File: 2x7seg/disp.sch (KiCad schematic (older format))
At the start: 11 parts, among them P1 CONN_01X08, P2 CONN_01X08, U1 TLC59282, U2 LDD-A814RI

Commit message: Adjust the pin drill size for the 7-seg display.
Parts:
- P1, P2: footprint Pin_Headers:Pin_Header_Straight_1x08 -> local:Pin_Header_1x08_edge
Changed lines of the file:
@@
 F 0 "P1" H 1200 2600 50  0000 C CNN
 F 1 "CONN_01X08" V 1300 2150 50  0000 C CNN
-F 2 "Pin_Headers:Pin_Header_Straight_1x08" H 1200 2150 60  0001 C CNN
+F 2 "local:Pin_Header_1x08_edge" H 1200 2150 60  0001 C CNN
 F 3 "" H 1200 2150 60  0000 C CNN
 	1    1200 2150
@@
 F 0 "P2" H 10500 2600 50  0000 C CNN
 F 1 "CONN_01X08" V 10600 2150 50  0000 C CNN
-F 2 "Pin_Headers:Pin_Header_Straight_1x08" H 10500 2150 60  0001 C CNN
+F 2 "local:Pin_Header_1x08_edge" H 10500 2150 60  0001 C CNN
 F 3 "" H 10500 2150 60  0000 C CNN
 	1    10500 2150

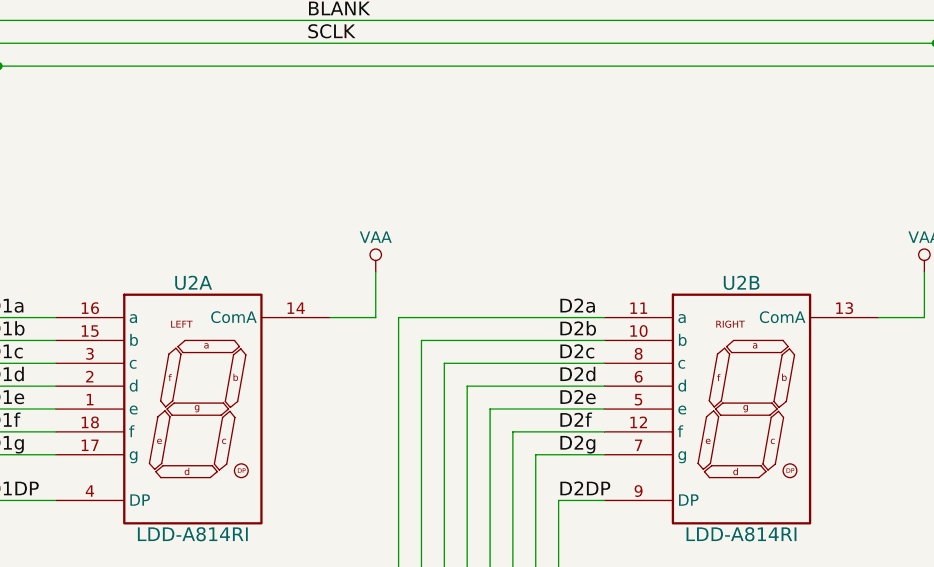
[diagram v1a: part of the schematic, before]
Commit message: Adjust the silk screen a little. Move some vias out of back silkscreen. Stitch in some more ground fill. Upload to OSHPark.
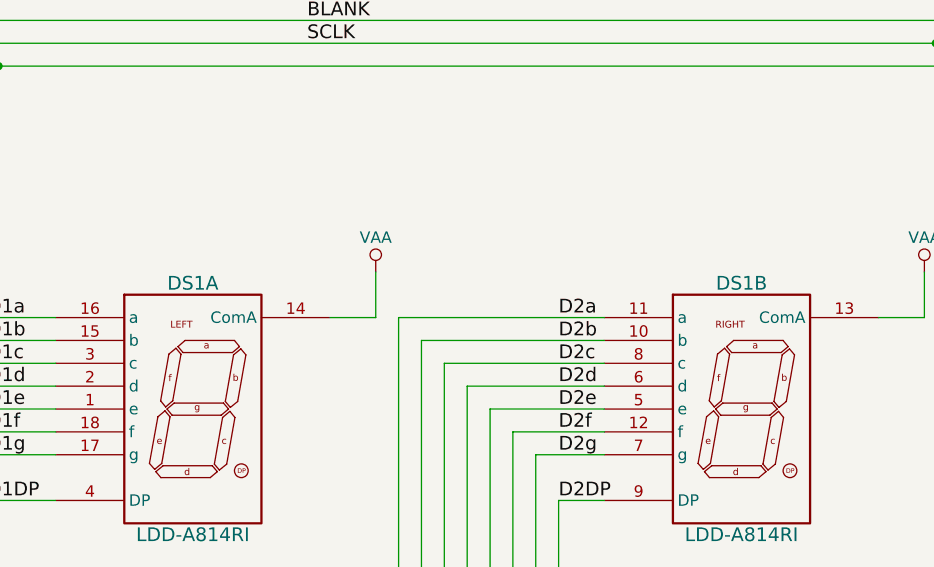
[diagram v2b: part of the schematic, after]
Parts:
- renumbered U2 to DS1
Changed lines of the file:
@@
 $EndComp
 $Comp
-L LDD-A814RI U2
+L LDD-A814RI DS1
 U 1 1 55975809
 P 6600 4000
-F 0 "U2" H 6600 4550 60  0000 C CNN
+F 0 "DS1" H 6600 4550 60  0000 C CNN
 F 1 "LDD-A814RI" H 6600 3450 60  0000 C CNN
 F 2 "local:LDD-A814RI" H 6600 4000 60  0001 C CNN
@@
 $EndComp
 $Comp
-L LDD-A814RI U2
+L LDD-A814RI DS1
 U 2 1 55975859
 P 9000 4000
-F 0 "U2" H 9000 4550 60  0000 C CNN
+F 0 "DS1" H 9000 4550 60  0000 C CNN
 F 1 "LDD-A814RI" H 9000 3450 60  0000 C CNN
 F 2 "local:LDD-A814RI" H 9000 4000 60  0001 C CNN
@@
 $EndComp
 $Comp
-L GND #PWR01
+L GND #PWR3
 U 1 1 55975CA2
 P 2300 5800
-F 0 "#PWR01" H 2300 5550 50  0001 C CNN
+F 0 "#PWR3" H 2300 5550 50  0001 C CNN
 F 1 "GND" H 2300 5650 50  0000 C CNN
 F 2 "" H 2300 5800 60  0000 C CNN
@@
 $EndComp
 $Comp
-L VCC #PWR02
+L VCC #PWR1
 U 1 1 55975CC2
 P 1800 1500
-F 0 "#PWR02" H 1800 1350 50  0001 C CNN
+F 0 "#PWR1" H 1800 1350 50  0001 C CNN
 F 1 "VCC" H 1800 1650 50  0000 C CNN
 F 2 "" H 1800 1500 60  0000 C CNN
@@
 	5800 7050 5800 7400
 $Comp
-L GND #PWR03
+L GND #PWR2
 U 1 1 5597FD15
 P 1800 2750
-F 0 "#PWR03" H 1800 2500 50  0001 C CNN
+F 0 "#PWR2" H 1800 2500 50  0001 C CNN
 F 1 "GND" H 1800 2600 50  0000 C CNN
 F 2 "" H 1800 2750 60  0000 C CNN
@@
 	2300 5500 2300 5800
 $Comp
-L GND #PWR04
+L GND #PWR6
 U 1 1 55980AD7
 P 4450 7400
-F 0 "#PWR04" H 4450 7150 50  0001 C CNN
+F 0 "#PWR6" H 4450 7150 50  0001 C CNN
 F 1 "GND" H 4450 7250 50  0000 C CNN
 F 2 "" H 4450 7400 60  0000 C CNN
@@
 Connection ~ 4450 7200
 $Comp
-L GND #PWR05
+L GND #PWR8
 U 1 1 55980ED3
 P 5800 7400
-F 0 "#PWR05" H 5800 7150 50  0001 C CNN
+F 0 "#PWR8" H 5800 7150 50  0001 C CNN
 F 1 "GND" H 5800 7250 50  0000 C CNN
 F 2 "" H 5800 7400 60  0000 C CNN
@@
 Connection ~ 5800 7200
 $Comp
-L VCC #PWR06
+L VCC #PWR5
 U 1 1 55981037
 P 4450 6400
-F 0 "#PWR06" H 4450 6250 50  0001 C CNN
+F 0 "#PWR5" H 4450 6250 50  0001 C CNN
 F 1 "VCC" H 4450 6550 50  0000 C CNN
 F 2 "" H 4450 6400 60  0000 C CNN
@@
 	8200 4400 8400 4400
 $Comp
-L VCC #PWR07
+L VCC #PWR11
 U 1 1 559820BB
 P 9850 1000
-F 0 "#PWR07" H 9850 850 50  0001 C CNN
+F 0 "#PWR11" H 9850 850 50  0001 C CNN
 F 1 "VCC" H 9850 1150 50  0000 C CNN
 F 2 "" H 9850 1000 60  0000 C CNN
@@
 $EndComp
 $Comp
-L GND #PWR08
+L GND #PWR12
 U 1 1 55982884
 P 10000 3350
-F 0 "#PWR08" H 10000 3100 50  0001 C CNN
+F 0 "#PWR12" H 10000 3100 50  0001 C CNN
 F 1 "GND" H 10000 3200 50  0000 C CNN
 F 2 "" H 10000 3350 60  0000 C CNN
@@
 Connection ~ 9850 2400
 $Comp
-L VAA #PWR09
+L VAA #PWR4
 U 1 1 559831F1
 P 3200 1500
-F 0 "#PWR09" H 3200 1350 50  0001 C CNN
+F 0 "#PWR4" H 3200 1350 50  0001 C CNN
 F 1 "VAA" H 3200 1650 50  0000 C CNN
 F 2 "" H 3200 1500 60  0000 C CNN
@@
 $EndComp
 $Comp
-L VAA #PWR010
+L VAA #PWR10
 U 1 1 559832E2
 P 9800 3400
-F 0 "#PWR010" H 9800 3250 50  0001 C CNN
+F 0 "#PWR10" H 9800 3250 50  0001 C CNN
 F 1 "VAA" H 9800 3550 50  0000 C CNN
 F 2 "" H 9800 3400 60  0000 C CNN
@@
 	9800 3600 9600 3600
 $Comp
-L VAA #PWR011
+L VAA #PWR7
 U 1 1 559842A3
 P 5800 6350
-F 0 "#PWR011" H 5800 6200 50  0001 C CNN
+F 0 "#PWR7" H 5800 6200 50  0001 C CNN
 F 1 "VAA" H 5800 6500 50  0000 C CNN
 F 2 "" H 5800 6350 60  0000 C CNN
@@
 Connection ~ 5800 6600
 $Comp
-L VAA #PWR012
+L VAA #PWR9
 U 1 1 559843C1
 P 7400 3400
-F 0 "#PWR012" H 7400 3250 50  0001 C CNN
+F 0 "#PWR9" H 7400 3250 50  0001 C CNN
 F 1 "VAA" H 7400 3550 50  0000 C CNN
 F 2 "" H 7400 3400 60  0000 C CNN
@@
 	7400 3600 7200 3600
 $Comp
-L PWR_FLAG #FLG013
+L PWR_FLAG #FLG1
 U 1 1 559854F7
 P 4700 1500
-F 0 "#FLG013" H 4700 1595 50  0001 C CNN
+F 0 "#FLG1" H 4700 1595 50  0001 C CNN
 F 1 "PWR_FLAG" H 4700 1680 50  0000 C CNN
 F 2 "" H 4700 1500 60  0000 C CNN
@@
 	4700 1500 4700 1800
 $Comp
-L PWR_FLAG #FLG014
+L PWR_FLAG #FLG2
 U 1 1 55985759
 P 5250 1500
-F 0 "#FLG014" H 5250 1595 50  0001 C CNN
+F 0 "#FLG2" H 5250 1595 50  0001 C CNN
 F 1 "PWR_FLAG" H 5250 1680 50  0000 C CNN
 F 2 "" H 5250 1500 60  0000 C CNN
@@
 $EndComp
 $Comp
-L PWR_FLAG #FLG015
+L PWR_FLAG #FLG3
 U 1 1 5598594E
 P 5750 1500
-F 0 "#FLG015" H 5750 1595 50  0001 C CNN
+F 0 "#FLG3" H 5750 1595 50  0001 C CNN
 F 1 "PWR_FLAG" H 5750 1680 50  0000 C CNN
 F 2 "" H 5750 1500 60  0000 C CNN

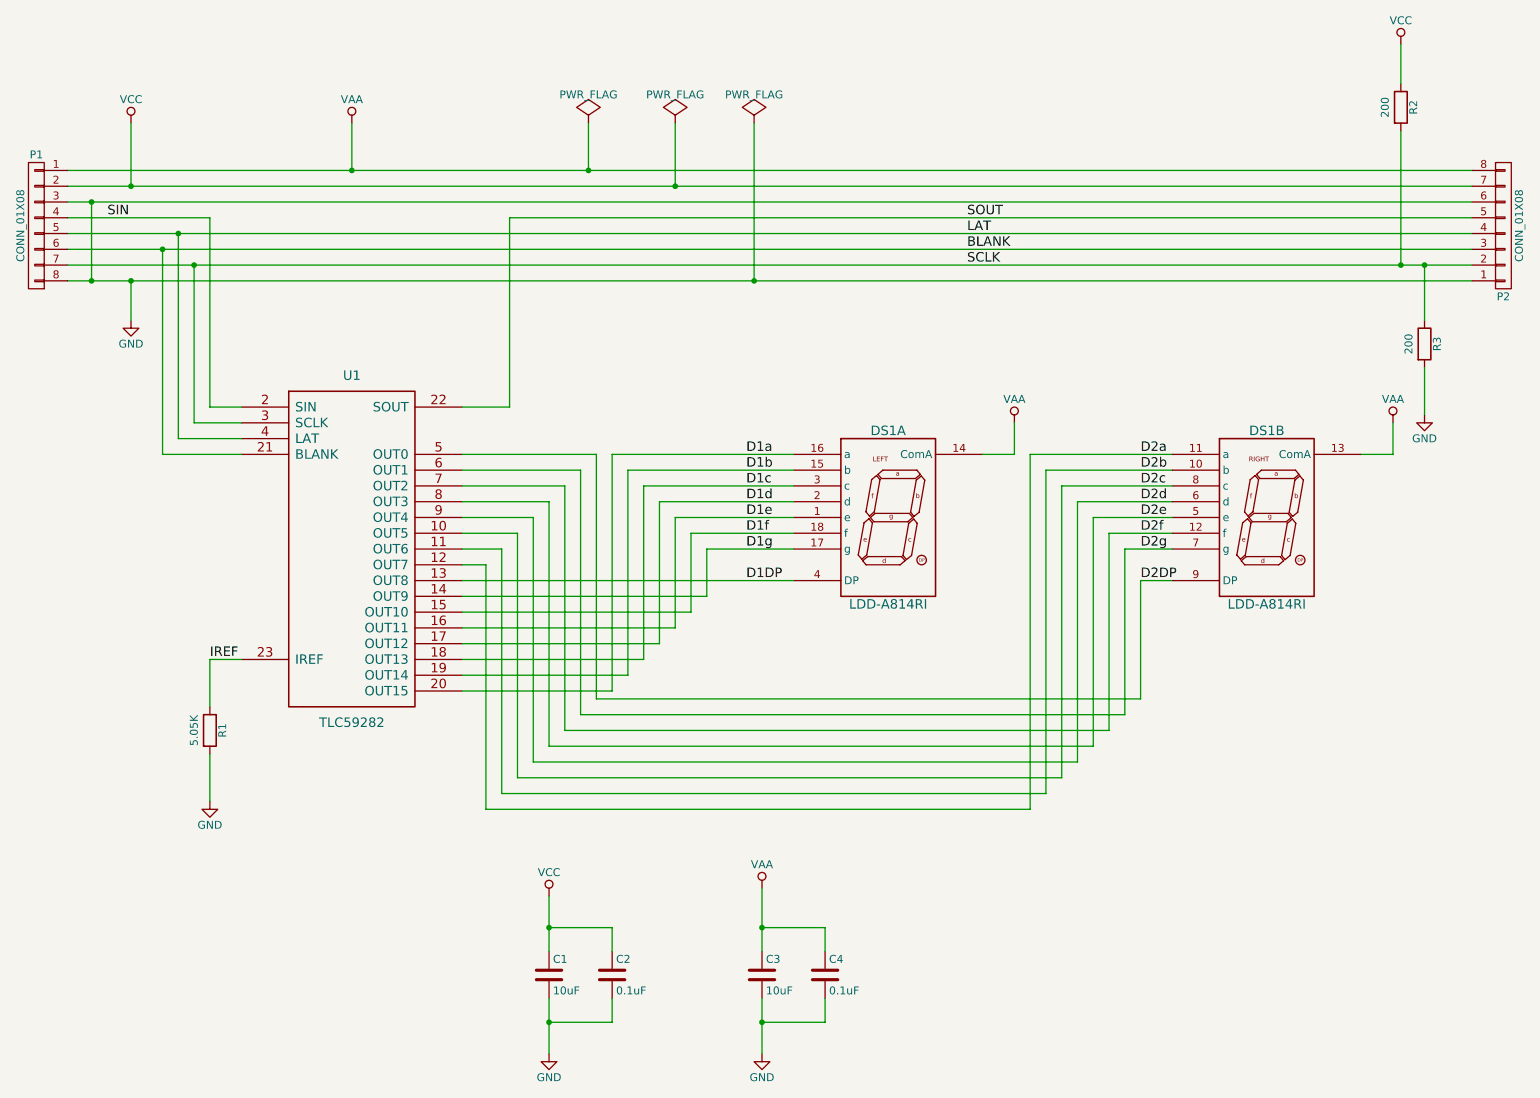
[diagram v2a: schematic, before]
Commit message: Use 1% resistor values
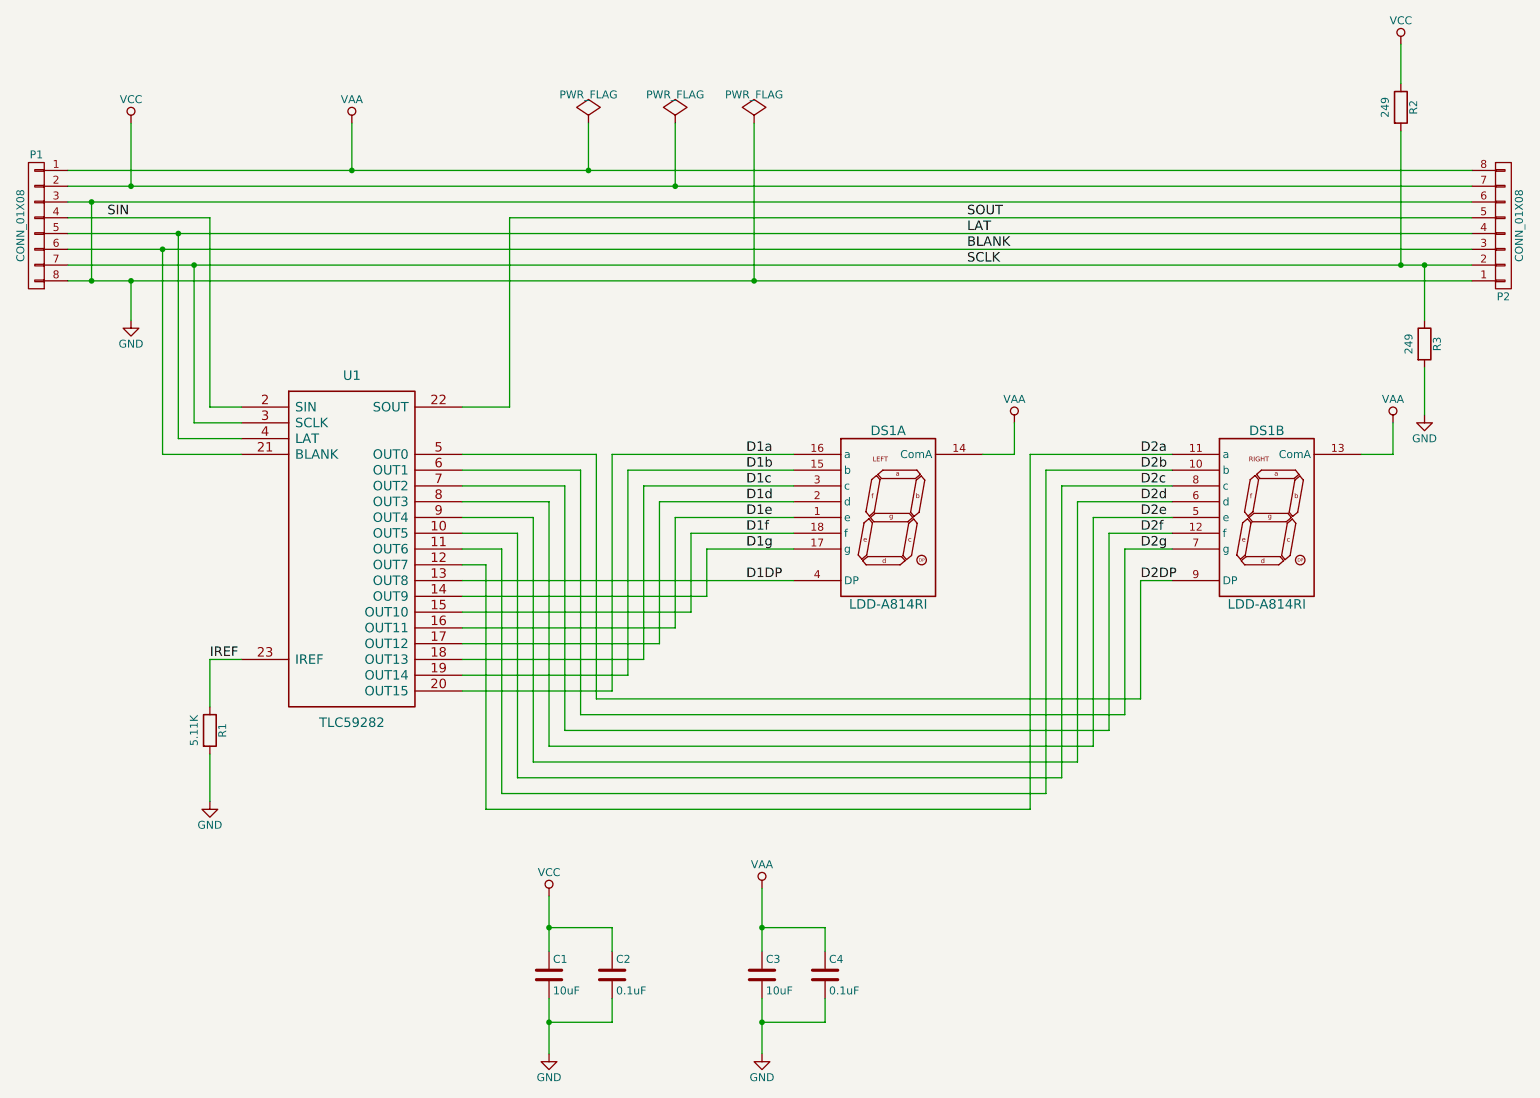
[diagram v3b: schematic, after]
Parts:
- R1: value 5.05K -> 5.11K
- R2, R3: value 200 -> 249
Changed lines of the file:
@@
 P 2300 5350
 F 0 "R1" V 2380 5350 50  0000 C CNN
-F 1 "5.05K" V 2200 5350 50  0000 C CNN
+F 1 "5.11K" V 2200 5350 50  0000 C CNN
 F 2 "Resistors_SMD:R_0805_HandSoldering" V 2230 5350 30  0001 C CNN
 F 3 "" H 2300 5350 30  0000 C CNN
@@
 P 10000 2900
 F 0 "R3" V 10080 2900 50  0000 C CNN
-F 1 "200" V 9900 2900 50  0000 C CNN
+F 1 "249" V 9900 2900 50  0000 C CNN
 F 2 "Resistors_SMD:R_0805_HandSoldering" V 9930 2900 30  0001 C CNN
 F 3 "" H 10000 2900 30  0000 C CNN
@@
 P 9850 1400
 F 0 "R2" V 9930 1400 50  0000 C CNN
-F 1 "200" V 9750 1400 50  0000 C CNN
+F 1 "249" V 9750 1400 50  0000 C CNN
 F 2 "Resistors_SMD:R_0805_HandSoldering" V 9780 1400 30  0001 C CNN
 F 3 "" H 9850 1400 30  0000 C CNN

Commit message: Next version of display board. Increase size of holes for display pins.
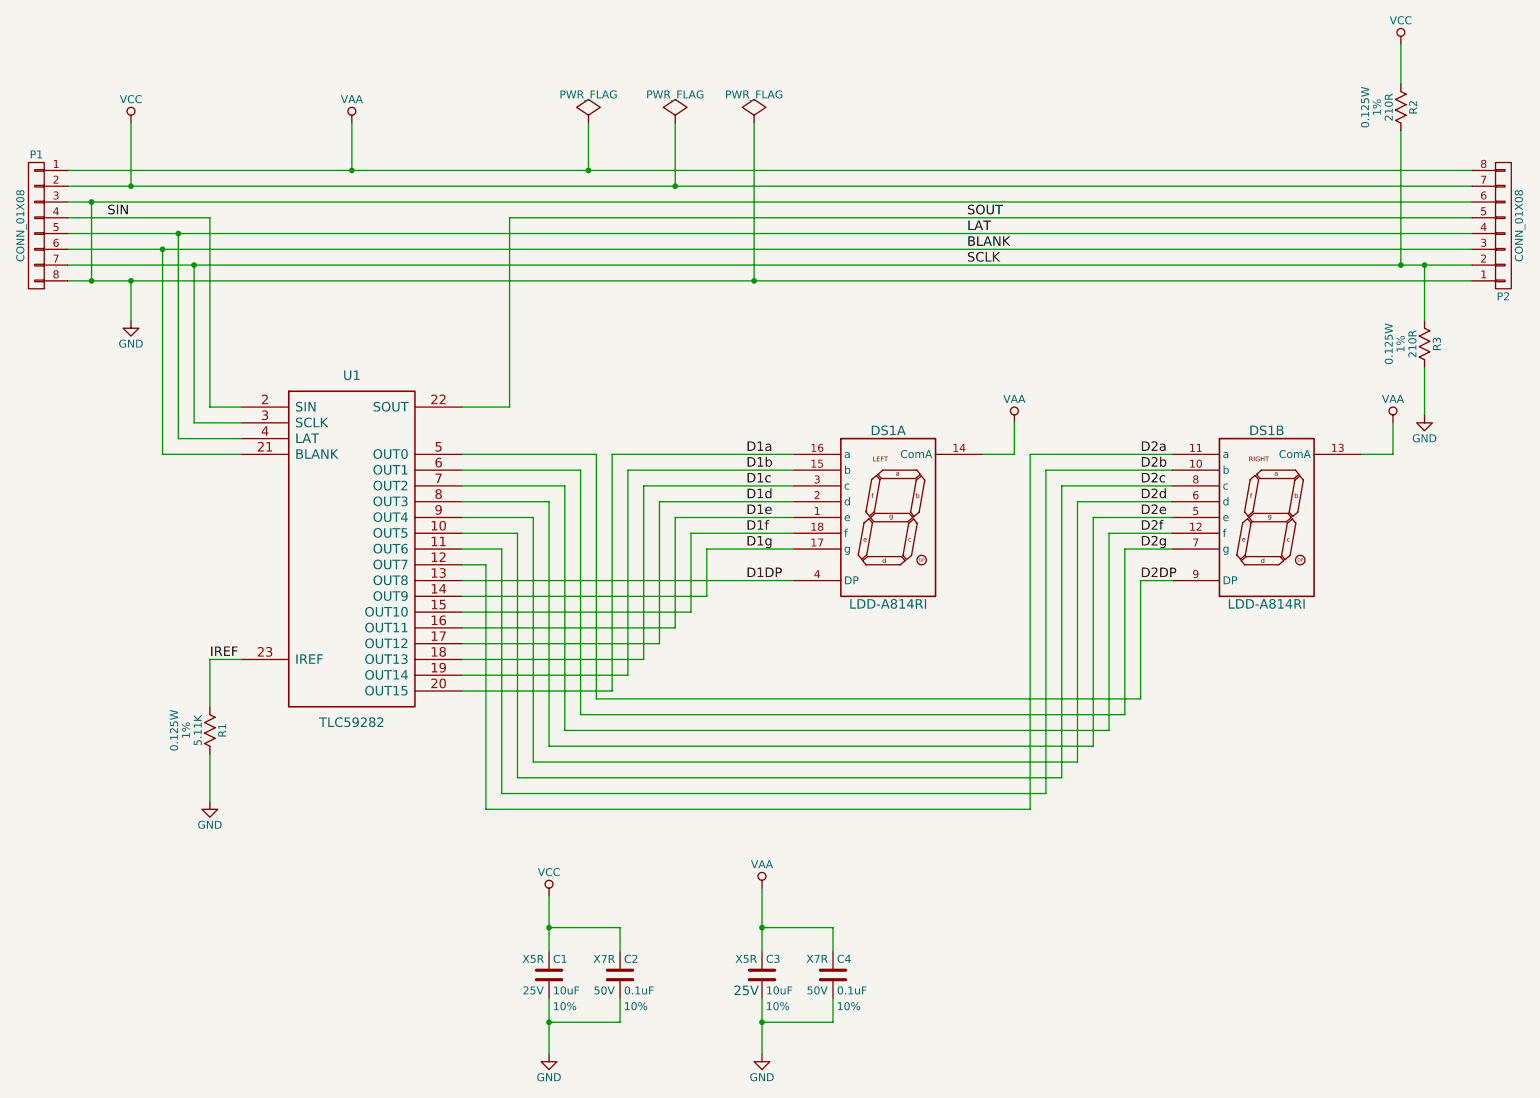
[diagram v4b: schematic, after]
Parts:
- removed R1: 5.11K, Resistors_SMD:R_0805_HandSoldering, symbol R
- removed R2, R3: 249, Resistors_SMD:R_0805_HandSoldering, symbol R
- added R1: 5.11K, Resistors_SMD:R_0805_HandSoldering, symbol R_local
- added R2, R3: 210R, Resistors_SMD:R_0805_HandSoldering, symbol R_local
- C1, C3: Dielectric (none) -> X5R; Manufacturer (none) -> TDK; PartNum (none) -> C3216X5R1E106K160AB; Tolerance (none) -> 10%; Voltage (none) -> 25V
- C2, C4: Dielectric (none) -> X7R; Manufacturer (none) -> Kemet; PartNum (none) -> C0805C104K5RACTU; Tolerance (none) -> 10%; Voltage (none) -> 50V
- DS1: Manufacturer (none) -> Lumex; PartNum (none) -> LDD-A814RI
- U1: Manufacturer (none) -> Texas Instruments; PartNum (none) -> TLC59282DBQ
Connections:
- net GND: now also R1.2, R3.2
- net IREF: now also R1.1
- net SCLK: now also R2.2, R3.1
- net VCC: now also R2.1
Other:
- moved on the sheet: C2
